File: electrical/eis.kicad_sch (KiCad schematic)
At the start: 25 parts

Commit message: Interim check-in
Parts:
- removed CHT1, CHT2, CHT3, CHT4, EGT1, EGT2, EGT3, EGT4, FUEL_FLOW, FUEL_LEFT, FUEL_RIGHT, MANIFOLD_PRESSURE, OIL_PRESSURE, OIL_TEMPERATURE, SHUNT: FUEL_QTY_SENSOR, symbol Device:R_Potentiometer
- removed FUEL_PRESSURE: ~, symbol flyerx:Kavlico_P4055
- removed PITCH_TRIM_POS: ~, symbol flyerx:Ray_Allen_POS-12
- added CHT1, CHT2, CHT3, CHT4, EGT1, EGT2, EGT3, EGT4, FUEL_LEFT, FUEL_RIGHT, OIL_TEMP: ~, symbol Device:R_Variable_US
- added CHT1P, CHT2P, CHT3P, CHT4P, EGT1P, EGT2P, EGT3P, EGT4P: ~, symbol Connector:Conn_01x02_Pin
- added CHT1R, CHT2R, CHT3R, CHT4R, EGT1R, EGT2R, EGT3R, EGT4R: ~, symbol Connector:Conn_01x02_Socket
- added COP: DTM6P, symbol Connector:Conn_01x06_Socket
- added COR: DTM6R, symbol Connector:Conn_01x06_Pin
- added FFP, FLAPP: DTM3P, symbol Connector:Conn_01x03_Socket
- added FFR, FLAPR: DTM3R, symbol Connector:Conn_01x03_Pin
- added FUEL_FLOW: FT-60, symbol flyerx:IE_FT-60
- added FUEL_PRESSURE: GPT 30G, symbol flyerx:Garmin_Sensor
- added LFP, RFP: Conn_01x01_Pin, symbol Connector:Conn_01x01_Pin
- added LFR, RFR: Conn_01x01_Socket, symbol Connector:Conn_01x01_Socket
- added MANIFOLD_PRESSURE: GPT 30A, symbol flyerx:Garmin_Sensor
- added OIL_PRESSURE: GPT 150G, symbol flyerx:Garmin_Sensor
- added OTP: DTM2P, symbol Connector:Conn_01x02_Socket
- added OTR: DTM2R, symbol Connector:Conn_01x02_Pin
- added TACH: UMA 1A3, symbol flyerx:UMA_1A3_Tachometer
- CO: value ~ -> Aithre 3.0
- FLAPS_POS: value ~ -> POS-12
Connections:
- net CAN_HI_IN is gone; now on net AMPS_HI: GEA24.P241_1 (CAN_HI)
- net CAN_LOW_IN is gone; now on net AMPS_LO: GEA24.P241_2 (CAN_LO)
- net EIS_SERIAL_IN is gone; now on net AMPS_HI: GEA24.P241_4 (RS-232_RX)
- net EIS_SERIAL_OUT is gone; now on net AMPS_LO: GEA24.P241_5 (RS-232_TX)
- net TACH1_GND is gone; now on net EIS_SERIAL_GND: GEA24.P243_7 (RPM_XDCR_GND_1)
- net TACH1_IN is gone; now on net AMPS_LO: GEA24.P243_8 (RPM_1)
- net TACH1_OUT is gone; now on net AMPS_HI: GEA24.P243_9 (RPM_XDCR_+12V_1)
- net EIS_SERIAL_GND: now also GEA24.P243_1 (FUEL_PRESS_GND), GEA24.P243_12 (MANIFOLD_PRESS_GND), GEA24.P243_16 (OIL_PRESS_GND), GEA24.P243_22 (FUEL_XDCR_GND_2), GEA24.P243_29 (POS_7/TIT_2/MISC_TEMP_2_HI), GEA24.P244_20 (GP1_LO/GND), GEA24.P244_23 (GP2_LO/GND), COR.4 (Pin_4), FFR.3 (Pin_3), FLAPR.3 (Pin_3), FUEL_PRESSURE.G (OUPUT), MANIFOLD_PRESSURE.B (GROUND), OIL_PRESSURE.B (GROUND), TACH.2 (GROUND)
- net Earth: now also FUEL_LEFT.1, FUEL_RIGHT.1
- net at GEA24.P242_20 (CHT3_HI): now also CHT3R.1 (Pin_1)
- net at GEA24.P242_8 (CHT3_LO): now also CHT3R.2 (Pin_2)
- net AMPS_HI: now reaches GEA24.P243_4 (FUEL_PRESS_XDCR_+5V)
- net AMPS_HI: now also GEA24.P243_15 (MANIFOLD_PRESS_XDCR_+5V), GEA24.P243_19 (OIL_PRESS_XDCR_+5V), GEA24.P243_24 (FUEL_XDCR_+12V_1), GEA24.P243_26 (GP+5V_1), GEA24.P243_33 (OIL_TEMP_HI), GEA24.P243_37 (SHUNT_1_HI), GEA24.P244_18 (GP1_HI/+5V), GEA24.P244_21 (GP2_HI/+5V), COR.1 (Pin_1), FFR.1 (Pin_1), FLAPR.1 (Pin_1), FUEL_PRESSURE.R (VIN), MANIFOLD_PRESSURE.R (VIN), OIL_PRESSURE.R (VIN), OTR.1 (Pin_1), TACH.1 (POWER_VSS)
- net AMPS_LO: now reaches GEA24.P243_2 (FUEL_PRESS)
- net AMPS_LO: now also GEA24.P243_13 (MANIFOLD_PRESS), GEA24.P243_23 (FUEL_FLOW), GEA24.P243_31 (POS_6/TIT_1/MISC_TEMP_1_HI), GEA24.P243_32 (OIL_TEMP_LO), GEA24.P243_36 (SHUNT_1_LO), GEA24.P244_19 (GP1/POS_1), GEA24.P244_22 (GP2/POS_2), COR.3 (Pin_3), FFR.2 (Pin_2), FLAPR.2 (Pin_2), FUEL_PRESSURE.B (GROUND), MANIFOLD_PRESSURE.G (OUPUT), OTR.2 (Pin_2), TACH.3 (SIGNAL_OUT)
- net at GEA24.P244_9 (FUEL_QTY_2): now also RFR.1 (Pin_1)
- net at GEA24.P242_22 (CHT2_HI): now also CHT2R.1 (Pin_1)
- net at GEA24.P242_10 (CHT2_LO): now also CHT2R.2 (Pin_2)
- net at GEA24.P242_23 (EGT_2_HI): now also EGT2R.1 (Pin_1)
- net at GEA24.P242_11 (EGT2_LO): now also EGT2R.2 (Pin_2)
- net at GEA24.P244_6 (FUEL_QTY_1): now also LFR.1 (Pin_1)
- net Red: now reaches GEA24.P242_12 (CHT1_LO)
- net Red: now also GEA24.P242_13 (EGT1_LO), CHT1R.2 (Pin_2), EGT1R.2 (Pin_2)
- net at GEA24.P242_18 (CHT4_HI): now also CHT4R.1 (Pin_1)
- net at GEA24.P242_19 (EGT4_HI): now also EGT4R.1 (Pin_1)
- net at GEA24.P242_21 (EGT3_HI): now also EGT3R.1 (Pin_1)
- net Yellow: now reaches GEA24.P242_24 (CHT1_HI)
- net Yellow: now also GEA24.P242_25 (EGT1_HI), CHT1R.1 (Pin_1), EGT1R.1 (Pin_1)
- net at GEA24.P242_6 (CHT4_LO): now also CHT4R.2 (Pin_2)
- net at GEA24.P242_7 (EGT4_LO): now also EGT4R.2 (Pin_2)
- net at GEA24.P242_9 (EGT3_LO): now also EGT3R.2 (Pin_2)
- net White/B/lue: now reaches GEA24.P243_17 (OIL_PRESS_HI)
- net White/B/lue: now also OIL_PRESSURE.G (OUPUT)
- net at CO.RED (+5V): now also COP.1 (Pin_1); no longer GEA24.P243_26 (GP+5V_1)
- net at CO.BLU (SPO2): now also COP.5 (Pin_5); no longer GEA24.P243_29 (POS_7/TIT_2/MISC_TEMP_2_HI)
- net at CO.WHT (CO): now also COP.3 (Pin_3); no longer GEA24.P243_31 (POS_6/TIT_1/MISC_TEMP_1_HI)
- net IGN_BAK_VOLTS: now reaches GEA24.P244_12 (POS_3/GP_3/FUEL_QTY_3)
- net at FLAPS_POS.O (+5V): now also FLAPP.2 (Pin_2); no longer GEA24.P244_21 (GP2_HI/+5V)
- net at FLAPS_POS.G (SENSE): now also FLAPP.1 (Pin_1); no longer GEA24.P244_22 (GP2/POS_2)
- net at FLAPS_POS.B (LOW): now also FLAPP.3 (Pin_3); no longer GEA24.P244_23 (GP2_LO/GND)
- net at CO.YLW (O2_PSI): now also COP.4 (Pin_4); no longer GEA24.P244_31 (POS_5/GP_5/FUEL_QTY_5)
- net FUEL_ON renamed IGN_BAK_LOW
- net TACH2_GND: no longer names the net of GEA24.P243_5 (RPM_XDCR_GND_2)
- net TACH2_IN: no longer names the net of GEA24.P243_6 (RPM_2)
- net TACH2_OUT: no longer names the net of GEA24.P243_10 (RPM_XDCR_+12V_2)
- new net: CHT1.2, CHT1P.1 (Pin_1)
- new net: CHT1.1, CHT1P.2 (Pin_2)
- new net: EGT3.1, EGT3P.2 (Pin_2)
- new net: EGT3.2, EGT3P.1 (Pin_1)
- new net: EGT4.1, EGT4P.2 (Pin_2)
- new net: EGT4.2, EGT4P.1 (Pin_1)
- new net: CHT3.2, CHT3P.1 (Pin_1)
- new net: CHT3.1, CHT3P.2 (Pin_2)
- new net: FFP.3 (Pin_3), FUEL_FLOW.B (GROUND)
- new net: FFP.1 (Pin_1), FUEL_FLOW.R (POWER)
- new net: FFP.2 (Pin_2), FUEL_FLOW.W (SIGNAL_OUT)
- new net: CHT4.2, CHT4P.1 (Pin_1)
- new net: CHT4.1, CHT4P.2 (Pin_2)
- new net: EGT1.1, EGT1P.2 (Pin_2)
- new net: EGT1.2, EGT1P.1 (Pin_1)
- new net: EGT2.2, EGT2P.1 (Pin_1)
- new net: EGT2.1, EGT2P.2 (Pin_2)
- new net: FUEL_RIGHT.2, RFP.1 (Pin_1)
- new net: CHT2.1, CHT2P.2 (Pin_2)
- new net: CHT2.2, CHT2P.1 (Pin_1)
- new net: CO.BLK (GROUND), COP.2 (Pin_2)
- new net: FUEL_LEFT.2, LFP.1 (Pin_1)
- new net: OIL_TEMP.2, OTP.1 (Pin_1)
- new net: OIL_TEMP.1, OTP.2 (Pin_2)
- new net White/Green: COR.2 (Pin_2), GEA24.P243_27 (GP_GND_1)
- new net White/Red: COR.5 (Pin_5), GEA24.P244_31 (POS_5/GP_5/FUEL_QTY_5)
- now unconnected: GEA24.P243_28 (POS_7/TIT_2/MISC_TEMP_2_LO), GEA24.P243_30 (POS_6/TIT_1/MISC_TEMP_1_LO), GEA24.P244_32 (POS_5_LO/GND)
- no-connect marks 47 -> 59
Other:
- note added: "Blade Connectors Wing Roots"
- note added: "Connector Built In"
- note added: "K Type Yellow Connectors"
- note added: "K-Type Yellow Connectors"
- note added: "Screw Terminal Connectors at Shunt"
- note removed: "Bendix"
- moved on the sheet: CO, FLAPS_POS

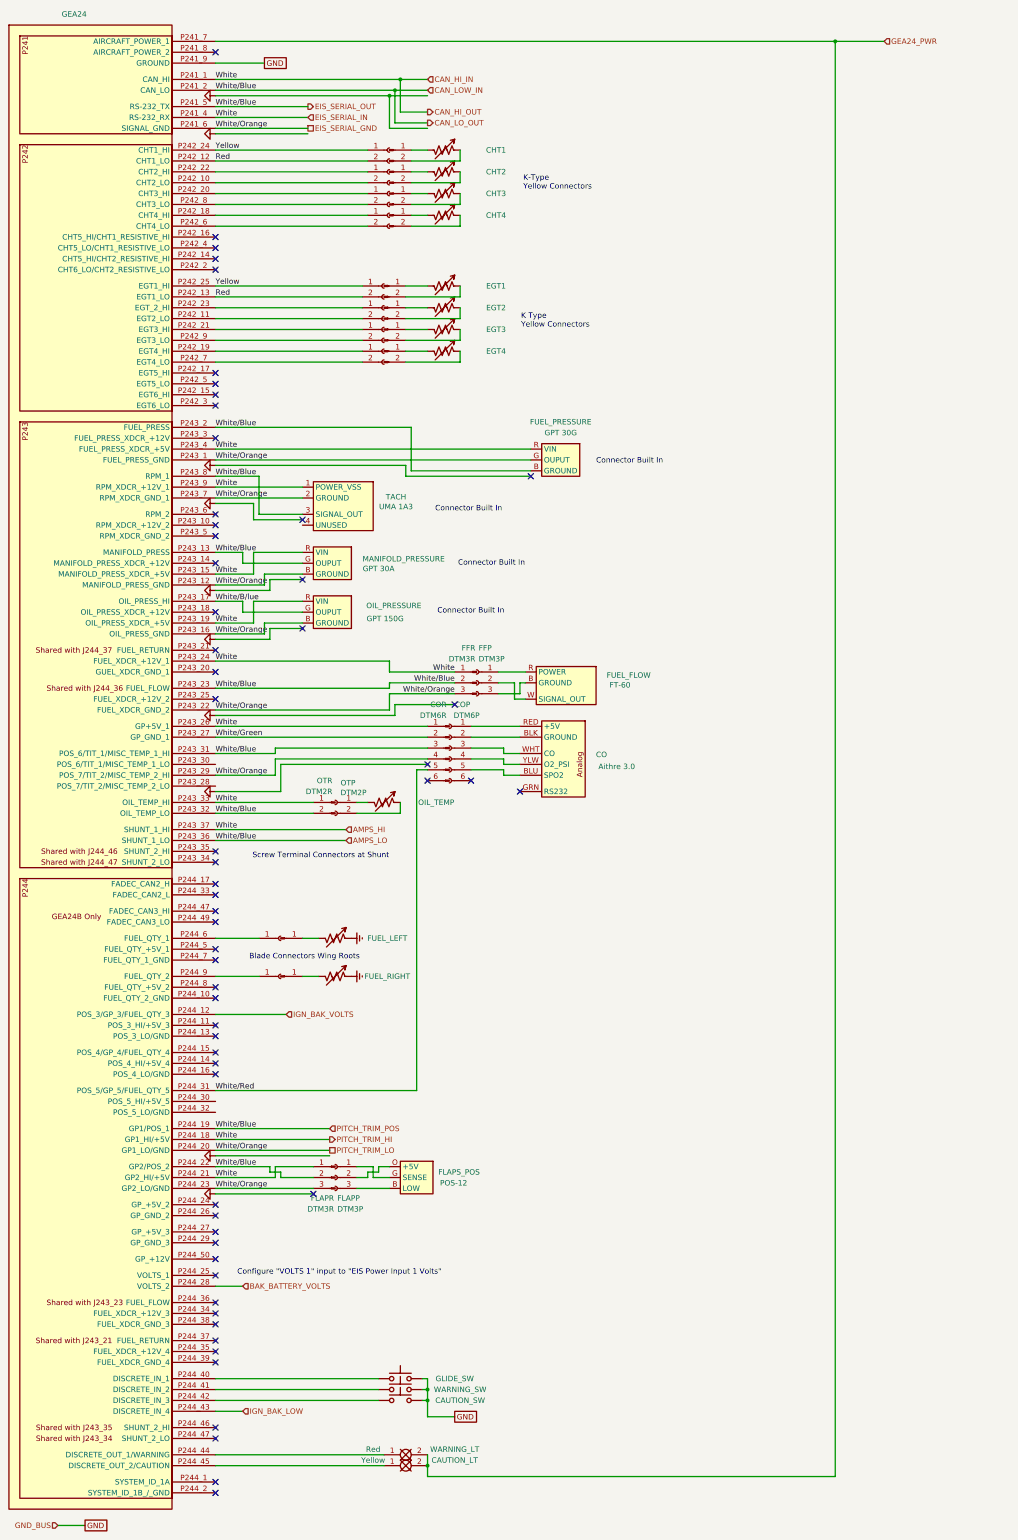
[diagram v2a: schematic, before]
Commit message: Went through and changed a lot from discussions and tradeoffs. Added GTX 330, rmemoved Connext from GDU and added to GPS 175 from GDL 52. Added relay for smoke and to not use GAD 27. Added Tach sensor for SureFly. Added carb heat. Added connectors to run panel disconnected.
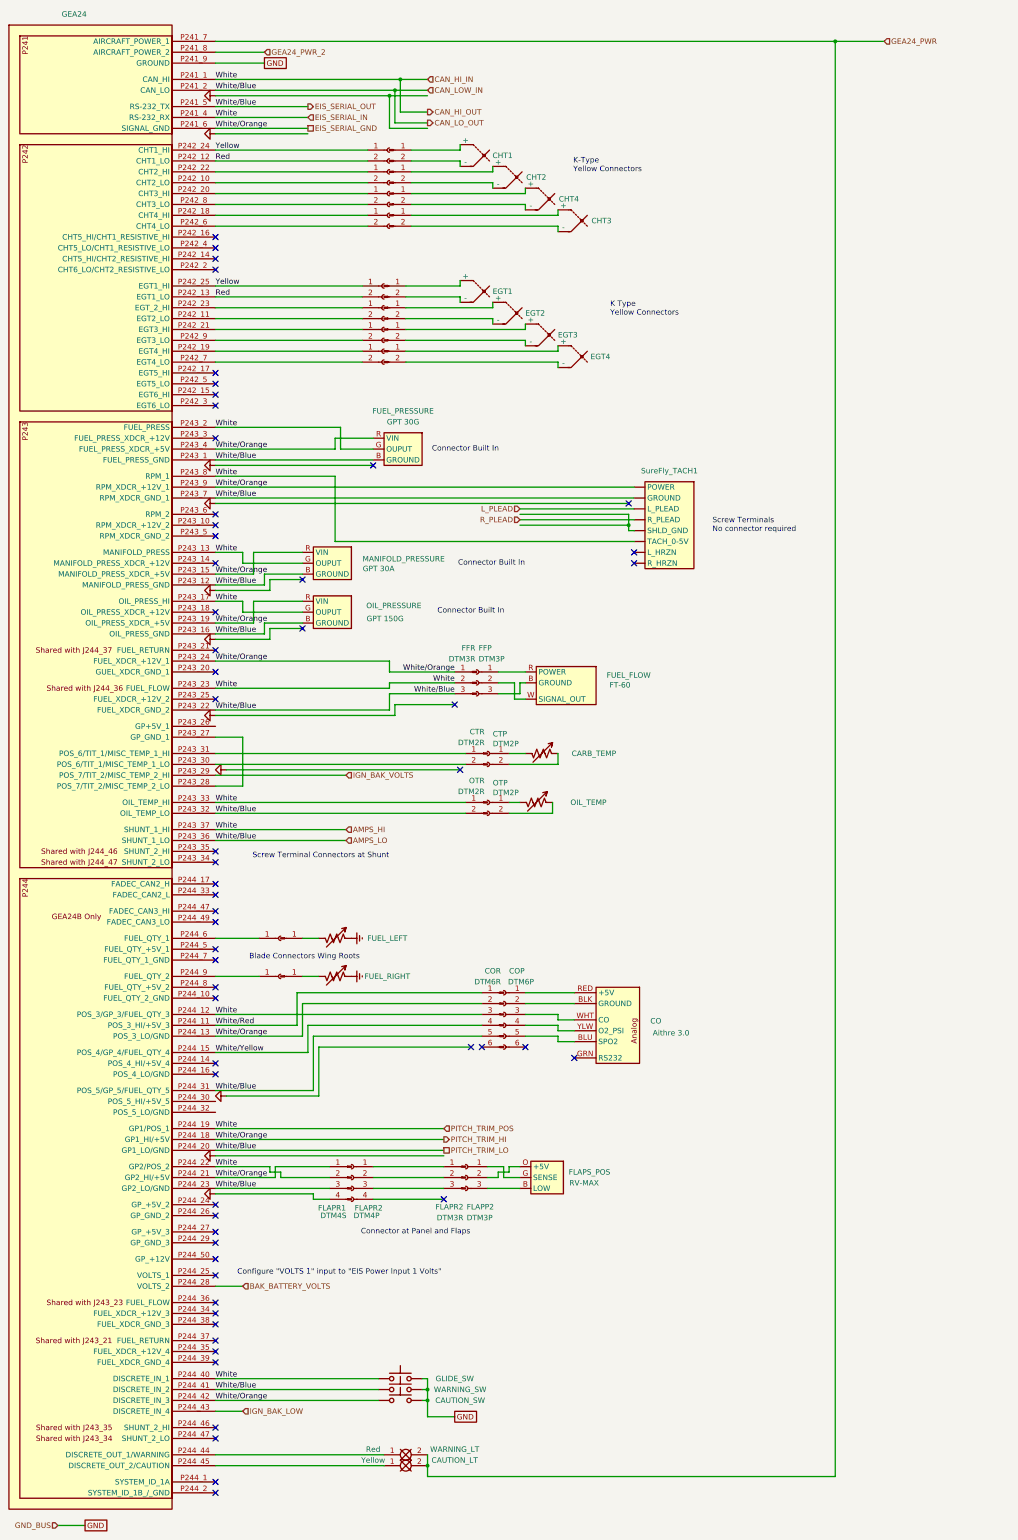
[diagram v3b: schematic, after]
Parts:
- removed CHT1, CHT2, CHT3, CHT4, EGT1, EGT2, EGT3, EGT4: ~, symbol Device:R_Variable_US
- removed TACH: UMA 1A3, symbol flyerx:UMA_1A3_Tachometer
- added CARB_TEMP: ~, symbol Device:R_Variable_US
- added CHT1, CHT2, CHT3, CHT4, EGT1, EGT2, EGT3, EGT4: Thermocouple, symbol Device:Thermocouple
- added CTP: DTM2P, symbol Connector:Conn_01x02_Socket
- added CTR: DTM2R, symbol Connector:Conn_01x02_Pin
- added FLAPR1: DTM4S, symbol Connector:Conn_01x04_Pin
- added FLAPR2: DTM4P, symbol Connector:Conn_01x04_Socket
- added SureFly_TACH1: ~, symbol flyerx:SureFly_TACH2
- FLAPS_POS: value POS-12 -> RV-MAX
- renumbered FLAPP to FLAPP2, FLAPR to FLAPR2
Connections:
- net White/B/lue is gone; now on net AMPS_HI: GEA24.P243_17 (OIL_PRESS_HI), OIL_PRESSURE.G (OUPUT)
- net AMPS_HI: now also COR.3 (Pin_3), FFR.2 (Pin_2), FUEL_PRESSURE.G (OUPUT), GEA24.P243_13 (MANIFOLD_PRESS), GEA24.P243_2 (FUEL_PRESS), GEA24.P243_23 (FUEL_FLOW), GEA24.P243_8 (RPM_1), GEA24.P244_12 (POS_3/GP_3/FUEL_QTY_3), GEA24.P244_19 (GP1/POS_1), GEA24.P244_22 (GP2/POS_2), GEA24.P244_40 (DISCRETE_IN_1), GLIDE_SW.1, MANIFOLD_PRESSURE.G (OUPUT), FLAPR1.2 (Pin_2), SureFly_TACH1. (R_HRZN); no longer COR.1 (Pin_1), FFR.1 (Pin_1), FLAPR2.1 (Pin_1), FUEL_PRESSURE.R (VIN), GEA24.P243_15 (MANIFOLD_PRESS_XDCR_+5V), GEA24.P243_19 (OIL_PRESS_XDCR_+5V), GEA24.P243_24 (FUEL_XDCR_+12V_1), GEA24.P243_26 (GP+5V_1), GEA24.P243_4 (FUEL_PRESS_XDCR_+5V), GEA24.P243_9 (RPM_XDCR_+12V_1), GEA24.P244_18 (GP1_HI/+5V), GEA24.P244_21 (GP2_HI/+5V), MANIFOLD_PRESSURE.R (VIN), OIL_PRESSURE.R (VIN)
- net AMPS_LO: now also COR.5 (Pin_5), FFR.3 (Pin_3), GEA24.P243_1 (FUEL_PRESS_GND), GEA24.P243_12 (MANIFOLD_PRESS_GND), GEA24.P243_16 (OIL_PRESS_GND), GEA24.P243_22 (FUEL_XDCR_GND_2), GEA24.P243_7 (RPM_XDCR_GND_1), GEA24.P244_20 (GP1_LO/GND), GEA24.P244_23 (GP2_LO/GND), GEA24.P244_31 (POS_5/GP_5/FUEL_QTY_5), GEA24.P244_41 (DISCRETE_IN_2), MANIFOLD_PRESSURE.B (GROUND), OIL_PRESSURE.B (GROUND), WARNING_SW.1, FLAPR1.3 (Pin_3), SureFly_TACH1. (R_HRZN); no longer COR.3 (Pin_3), FFR.2 (Pin_2), FLAPR2.2 (Pin_2), GEA24.P243_13 (MANIFOLD_PRESS), GEA24.P243_2 (FUEL_PRESS), GEA24.P243_23 (FUEL_FLOW), GEA24.P243_31 (POS_6/TIT_1/MISC_TEMP_1_HI), GEA24.P243_8 (RPM_1), GEA24.P244_19 (GP1/POS_1), GEA24.P244_22 (GP2/POS_2), MANIFOLD_PRESSURE.G (OUPUT)
- net EIS_SERIAL_GND: now also CAUTION_SW.1, COR.2 (Pin_2), FFR.1 (Pin_1), FUEL_PRESSURE.R (VIN), GEA24.P243_15 (MANIFOLD_PRESS_XDCR_+5V), GEA24.P243_19 (OIL_PRESS_XDCR_+5V), GEA24.P243_24 (FUEL_XDCR_+12V_1), GEA24.P243_4 (FUEL_PRESS_XDCR_+5V), GEA24.P243_9 (RPM_XDCR_+12V_1), GEA24.P244_13 (POS_3_LO/GND), GEA24.P244_18 (GP1_HI/+5V), GEA24.P244_21 (GP2_HI/+5V), GEA24.P244_42 (DISCRETE_IN_3), MANIFOLD_PRESSURE.R (VIN), OIL_PRESSURE.R (VIN), FLAPR1.1 (Pin_1), SureFly_TACH1. (R_HRZN); no longer COR.4 (Pin_4), FFR.3 (Pin_3), FLAPR2.3 (Pin_3), FUEL_PRESSURE.G (OUPUT), GEA24.P243_1 (FUEL_PRESS_GND), GEA24.P243_12 (MANIFOLD_PRESS_GND), GEA24.P243_16 (OIL_PRESS_GND), GEA24.P243_22 (FUEL_XDCR_GND_2), GEA24.P243_29 (POS_7/TIT_2/MISC_TEMP_2_HI), GEA24.P243_7 (RPM_XDCR_GND_1), GEA24.P244_20 (GP1_LO/GND), GEA24.P244_23 (GP2_LO/GND), MANIFOLD_PRESSURE.B (GROUND), OIL_PRESSURE.B (GROUND)
- net GNDS: now also FLAPR1.4 (Pin_4)
- net IGN_BAK_VOLTS: now also GEA24.P243_29 (POS_7/TIT_2/MISC_TEMP_2_HI); no longer GEA24.P244_12 (POS_3/GP_3/FUEL_QTY_3)
- net White/Red: now also COR.1 (Pin_1), GEA24.P244_11 (POS_3_HI/+5V_3); no longer COR.5 (Pin_5), GEA24.P244_31 (POS_5/GP_5/FUEL_QTY_5)
- net at CHT1P.1 (Pin_1): now also CHT1.1 (+)
- net at CHT1P.2 (Pin_2): now also CHT1.2 (-)
- net at EGT3P.2 (Pin_2): now also EGT3.2 (-)
- net at EGT3P.1 (Pin_1): now also EGT3.1 (+)
- net at EGT4P.2 (Pin_2): now also EGT4.2 (-)
- net at EGT4P.1 (Pin_1): now also EGT4.1 (+)
- net at CHT3P.1 (Pin_1): now also CHT4.1 (+)
- net at CHT3P.2 (Pin_2): now also CHT4.2 (-)
- net at CHT4P.1 (Pin_1): now also CHT3.1 (+)
- net at CHT4P.2 (Pin_2): now also CHT3.2 (-)
- net at EGT1P.2 (Pin_2): now also EGT1.2 (-)
- net at EGT1P.1 (Pin_1): now also EGT1.1 (+)
- net GEA24_PWR_2: now reaches GEA24.P241_8 (AIRCRAFT_POWER_2)
- net at GEA24.P243_28 (POS_7/TIT_2/MISC_TEMP_2_LO): now also GEA24.P243_27 (GP_GND_1)
- net at GEA24.P243_30 (POS_6/TIT_1/MISC_TEMP_1_LO): now also CTR.2 (Pin_2)
- net White/Yellow: now reaches GEA24.P244_15 (POS_4/GP_4/FUEL_QTY_4)
- net White/Yellow: now also COR.4 (Pin_4)
- net at EGT2P.1 (Pin_1): now also EGT2.1 (+)
- net at EGT2P.2 (Pin_2): now also EGT2.2 (-)
- net at CHT2P.2 (Pin_2): now also CHT2.2 (-)
- net at CHT2P.1 (Pin_1): now also CHT2.1 (+)
- removed net White/Green: COR.2 (Pin_2), GEA24.P243_27 (GP_GND_1)
- new net: CARB_TEMP.1, CTP.2 (Pin_2)
- new net: CARB_TEMP.2, CTP.1 (Pin_1)
- new net: FLAPR2.1 (Pin_1), FLAPR2.1 (Pin_1)
- new net: FLAPR2.2 (Pin_2), FLAPR2.2 (Pin_2)
- new net: FLAPR2.3 (Pin_3), FLAPR2.3 (Pin_3)
- new net: CTR.1 (Pin_1), GEA24.P243_31 (POS_6/TIT_1/MISC_TEMP_1_HI)
- new net L_PLEAD: SureFly_TACH1. (R_HRZN)
- new net R_PLEAD: SureFly_TACH1. (R_HRZN)
- no-connect marks 59 -> 58
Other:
- note added: "Connector at Panel and Flaps"
- note added: "Screw Terminals No connector required"
- moved on the sheet: CO, COP, COR, FLAPP2, FLAPR2, FLAPS_POS, FUEL_PRESSURE, OIL_TEMP, OTP, OTR

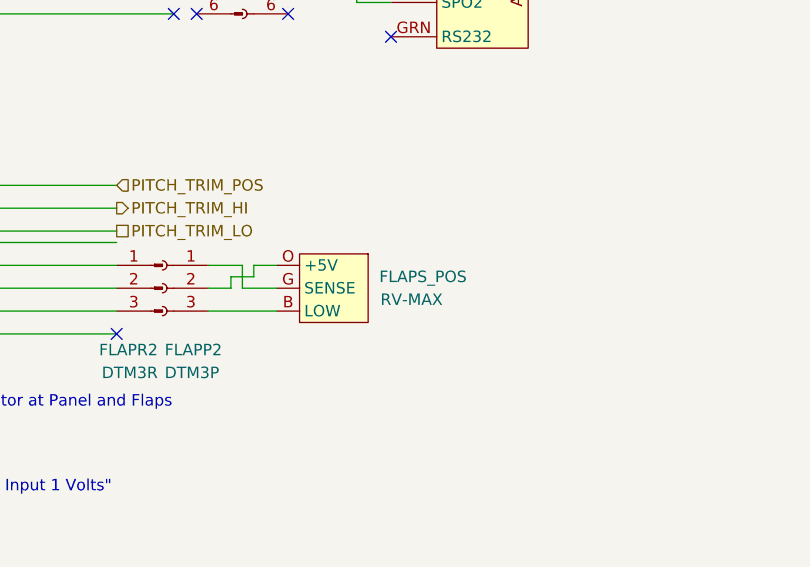
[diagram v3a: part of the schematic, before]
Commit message: Added beacon and added colors for flaps
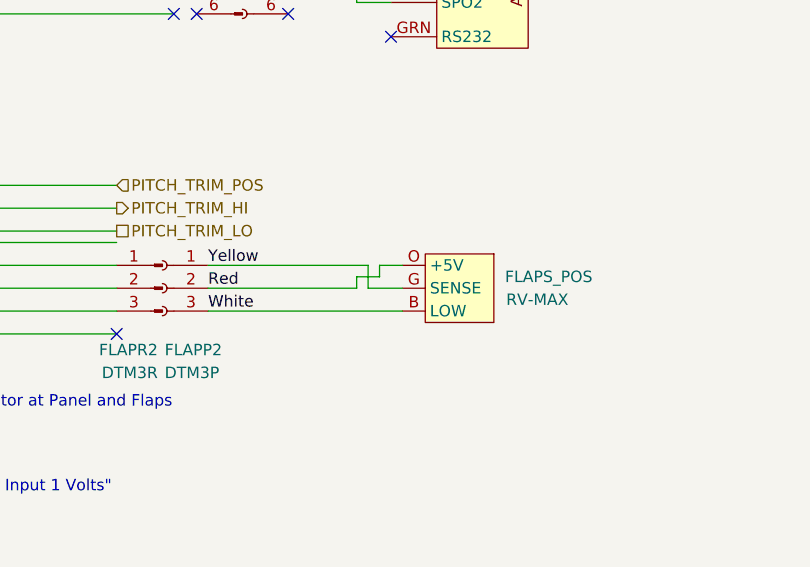
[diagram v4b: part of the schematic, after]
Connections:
- net AMPS_HI: now also FLAPP2.3 (Pin_3), FLAPS_POS.B (LOW)
- net Red: now also FLAPP2.2 (Pin_2), FLAPS_POS.O (+5V)
- net Yellow: now also FLAPP2.1 (Pin_1), FLAPS_POS.G (SENSE)
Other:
- moved on the sheet: FLAPS_POS
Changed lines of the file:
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@@
 	(title_block
 		(title "EIS")
-		(date "2025-12-24")
-		(rev "1.2")
+		(date "2026-01-01")
+		(rev "1.2.3")
 		(company "N877RV")
 	)
@@
 	(wire
 		(pts
-			(xy 134.62 287.02) (xy 138.43 287.02)
+			(xy 148.59 287.02) (xy 152.4 287.02)
 		)
 		(stroke
@@
 	(wire
 		(pts
-			(xy 134.62 284.48) (xy 134.62 287.02)
+			(xy 148.59 284.48) (xy 148.59 287.02)
 		)
 		(stroke
@@
 	(wire
 		(pts
-			(xy 133.35 285.75) (xy 135.89 285.75)
+			(xy 147.32 285.75) (xy 149.86 285.75)
 		)
 		(stroke
@@
 	(wire
 		(pts
-			(xy 130.81 289.56) (xy 138.43 289.56)
+			(xy 130.81 289.56) (xy 152.4 289.56)
 		)
 		(stroke
@@
 	(wire
 		(pts
-			(xy 130.81 284.48) (xy 134.62 284.48)
+			(xy 130.81 284.48) (xy 148.59 284.48)
 		)
 		(stroke
@@
 	(wire
 		(pts
-			(xy 133.35 287.02) (xy 133.35 285.75)
+			(xy 147.32 287.02) (xy 147.32 285.75)
 		)
 		(stroke
@@
 	(wire
 		(pts
-			(xy 135.89 284.48) (xy 138.43 284.48)
+			(xy 149.86 284.48) (xy 152.4 284.48)
 		)
 		(stroke
@@
 	(wire
 		(pts
-			(xy 130.81 287.02) (xy 133.35 287.02)
+			(xy 130.81 287.02) (xy 147.32 287.02)
 		)
 		(stroke
@@
 	(wire
 		(pts
-			(xy 135.89 285.75) (xy 135.89 284.48)
+			(xy 149.86 285.75) (xy 149.86 284.48)
 		)
 		(stroke
@@
 		)
 	)
+	(label "Red"
+		(at 130.81 287.02 0)
+		(effects
+			(font
+				(size 1.27 1.27)
+			)
+			(justify left bottom)
+		)
+	)
 	(label "White{slash}Blue"
 		(at 67.31 36.83 0)
@@
 		)
 	)
+	(label "White"
+		(at 130.81 289.56 0)
+		(effects
+			(font
+				(size 1.27 1.27)
+			)
+			(justify left bottom)
+		)
+	)
 	(label "White{slash}Orange"
 		(at 67.31 166.37 0)
@@
 		)
 	)
+	(label "Yellow"
+		(at 130.81 284.48 0)
+		(effects
+			(font
+				(size 1.27 1.27)
+			)
+			(justify left bottom)
+		)
+	)
 	(label "White{slash}Blue"
 		(at 67.31 160.02 0)
@@
 	(symbol
 		(lib_id "flyerx:Ray_Allen_POS-12")
-		(at 148.59 283.21 0)
+		(at 162.56 283.21 0)
 		(mirror y)
 		(unit 1)
@@
 		(dnp no)
 		(property "Reference" "FLAPS_POS"
-			(at 154.686 285.75 0)
+			(at 168.656 285.75 0)
 			(effects
 				(font
@@
 		)
 		(property "Value" "RV-MAX"
-			(at 153.416 288.29 0)
+			(at 167.386 288.29 0)
 			(effects
 				(font
@@
 		)
 		(property "Footprint" ""
-			(at 154.94 280.67 0)
+			(at 168.91 280.67 0)
 			(effects
 				(font
@@
 		)
 		(property "Datasheet" ""
-			(at 154.94 280.67 0)
+			(at 168.91 280.67 0)
 			(effects
 				(font
@@
 		)
 		(property "Description" ""
-			(at 148.59 283.21 0)
+			(at 162.56 283.21 0)
 			(effects
 				(font
